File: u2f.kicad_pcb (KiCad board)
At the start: 2 copper layers, 8 parts, among them P1 Touch Button, P2 V33prog, P3 D- prog, P4 USB_A, U1 ch552T

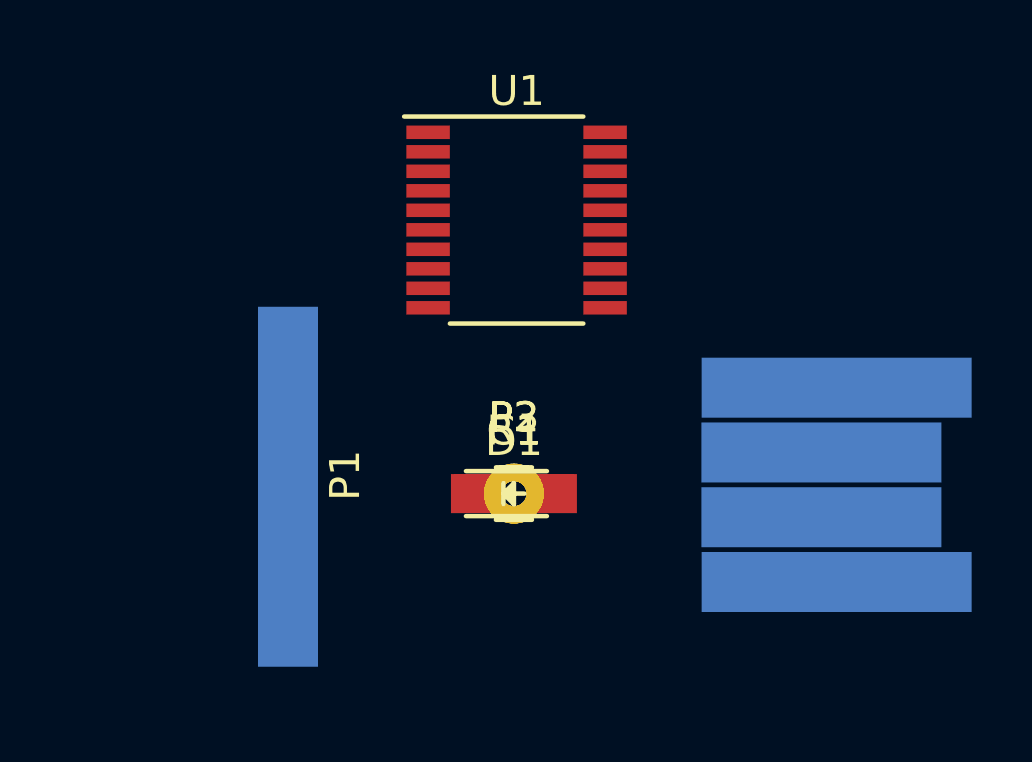
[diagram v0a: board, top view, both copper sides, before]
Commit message: checking in code for tonight. It's def. not perfect I've removed pins from the IC footprint. The fact that this is a bad practice is not lost on me
I just need to re-route power and GND so that the USB actually fits the correct dimensions.

Once that is done I will work on edge cuts and look at some boardhouses to see who is willing to make this
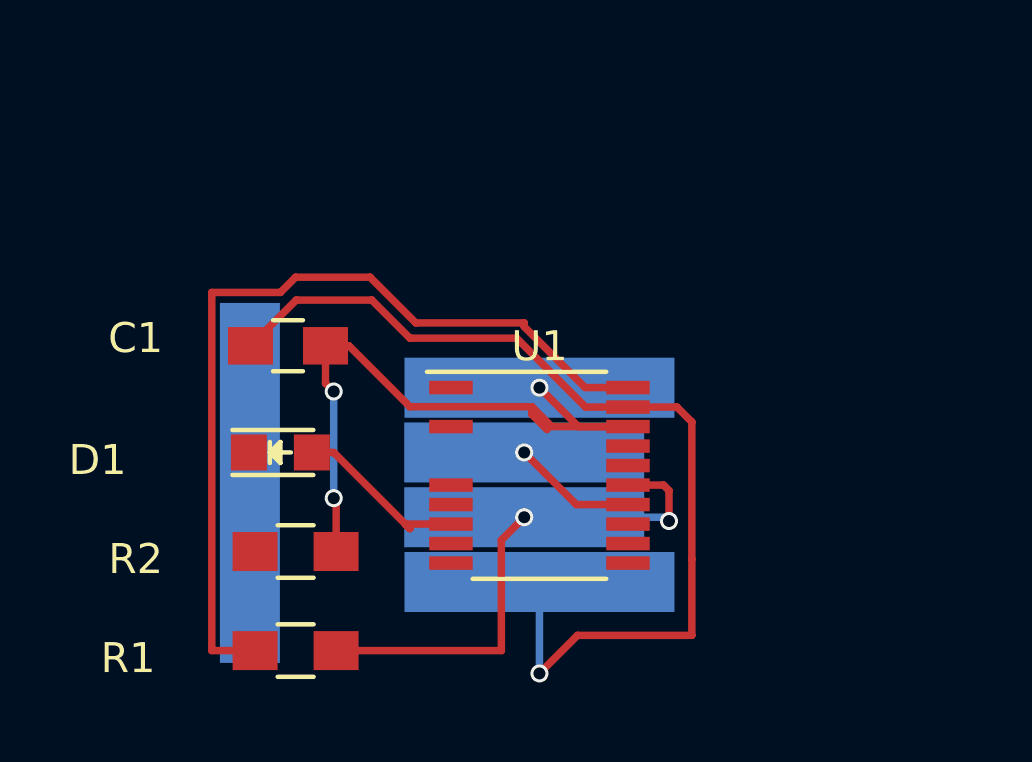
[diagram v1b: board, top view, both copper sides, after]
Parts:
- removed P2: V33prog, Wire_Pads:SolderWirePad_single_0-8mmDrill
- removed P3: D- prog, Wire_Pads:SolderWirePad_single_0-8mmDrill
- added R2: R, Resistors_SMD:R_0805_HandSoldering, F.Cu at (141.2, 106.9)
- P1, P4: moved to B.Cu
- moved P4 9.91 mm to (148.8, 104.6)
- moved C1 9.00 mm to (141.0, 100.1)
- moved R1 8.96 mm to (141.2, 110.2)
- moved U1 8.54 mm to (149.4, 104.4)
- moved D1 7.91 mm to (140.7, 103.6)
- moved P1 1.28 mm to (139.7, 104.6), turned to 270 degrees
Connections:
- D1 pad 1: GND -> Net-(D1-Pad1)
- R1 pad 1: Net-(P3-Pad1) -> Net-(R1-Pad1)
- U1 pad 13: Net-(D1-Pad2) -> Net-(U1-Pad13)
- U1 pad 20: Net-(P2-Pad1) -> Net-(R1-Pad1)
- U1 pad 8: Net-(U1-Pad8) -> Net-(D1-Pad2)
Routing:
- net +5V: track 0.00 -> 32.8 mm, vias 0 -> 1
- net Net-(R1-Pad1): track 0.00 -> 29.1 mm
- net GND: track 0.00 -> 22.7 mm, vias 0 -> 3
- net Net-(P4-Pad2): track 0.00 -> 17.6 mm, vias 0 -> 2
- net Net-(D1-Pad2): track 0.00 -> 6.06 mm
- net Net-(P4-Pad3): track 0.00 -> 4.18 mm, vias 0 -> 1

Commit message: made the traces a little better. I think I should rotate one of the resistors to avoid some of that wire jumping-around, but I guess it'll work
If it becomes a problem later I'll fix it.

I'll place the order for these boards after I get started working on the software. I want to be ready in the unlikely case that I need more pins or sometihng. Otherwise, I think I'll just internall pull resistors for the USB config and stuff

The first order will just be a test batch for functionality, then I'll actually clean up my design so it looks less like absolute shit and then do another prototype run followed by a bulk run
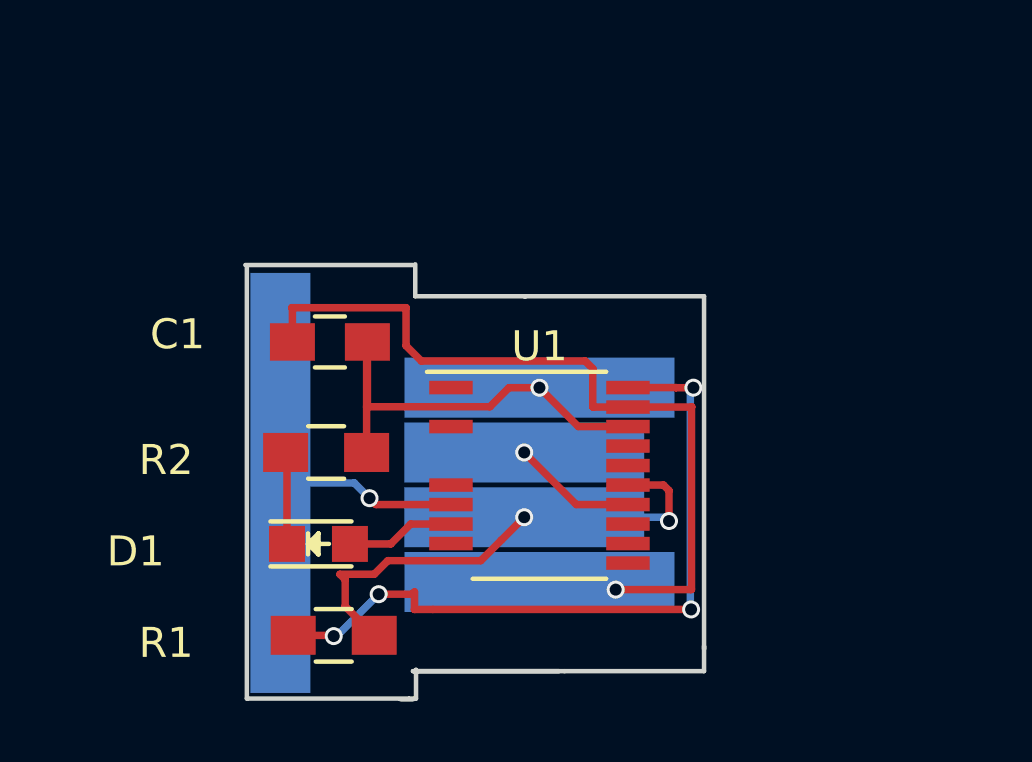
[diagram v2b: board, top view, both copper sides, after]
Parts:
- moved R2 3.45 mm to (142.2, 103.6)
- moved D1 3.30 mm to (142.0, 106.7)
- moved C1 1.40 mm to (142.4, 99.9)
- moved R1 1.37 mm to (142.5, 109.7)
- moved P1 1.02 mm to (140.7, 104.6)
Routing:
- net GND: track 22.7 -> 15.4 mm, vias 3 -> 1
- net Net-(P1-Pad1): track 0.00 -> 5.98 mm, vias 0 -> 1
- net Net-(R1-Pad1): track 29.1 -> 24.1 mm, vias 0 -> 4
- net +5V: track 32.8 -> 28.6 mm
- net Net-(D1-Pad1): track 0.43 -> 3.07 mm
- net Net-(D1-Pad2): track 6.06 -> 3.64 mm
- net Net-(P4-Pad2): track 17.6 -> 16.8 mm
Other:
- board outline added: 15.3 x 14.5 mm
